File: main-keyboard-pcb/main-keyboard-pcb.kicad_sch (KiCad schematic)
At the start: 174 parts, among them IC1 LMR51420XDDCR, J1 Debug SWD Connector, J2 Hotplug, J3 USB_B_Micro, SW1 SW_Push, SW10 SW_Push, SW11 SW_Push, SW12 SW_Push, SW13 SW_Push, SW14 SW_Push, SW15 SW_Push, SW16 SW_Push, SW17 SW_Push, SW18 SW_Push, SW19 SW_Push, SW2 SW_Push, SW20 SW_Push, SW21 SW_Push, SW22 SW_Push, SW23 SW_Push, SW24 SW_Push, SW25 SW_Push, SW26 SW_Push, SW27 SW_Push, SW28 SW_Push, SW29 SW_Push, SW3 SW_Push, SW30 SW_Push, SW31 SW_Push, SW32 SW_Push, SW33 SW_Push, SW34 SW_Push, SW35 SW_Push, SW36 SW_Push, SW37 SW_Push, SW38 SW_Push, SW39 SW_Push, SW4 SW_Push, SW40 SW_Push, SW41 SW_Push, SW42 SW_Push, SW43 SW_Push, SW44 SW_Push, SW45 SW_Push, SW46 SW_Push, SW47 SW_Push, SW48 SW_Push, SW49 SW_Push, SW5 SW_Push, SW50 SW_Push, SW51 SW_Push, SW52 SW_Push, SW53 SW_Push, SW54 SW_Push, SW55 SW_Push, SW56 SW_Push, SW57 SW_Push, SW58 SW_Push, SW59 SW_Push, SW6 SW_Push, SW60 SW_Push, SW61 SW_Push, SW62 SW_Push, SW63 SW_Push, SW64 SW_Push, SW65 SW_Push, SW66 SW_Push, SW67 SW_Push, SW7 SW_Push, SW8 SW_Push, SW9 SW_Push, SW99 SW_SPDT, U1 USBLC6-4SC6, U2 STM32F407VGT6, Y1 16MHz

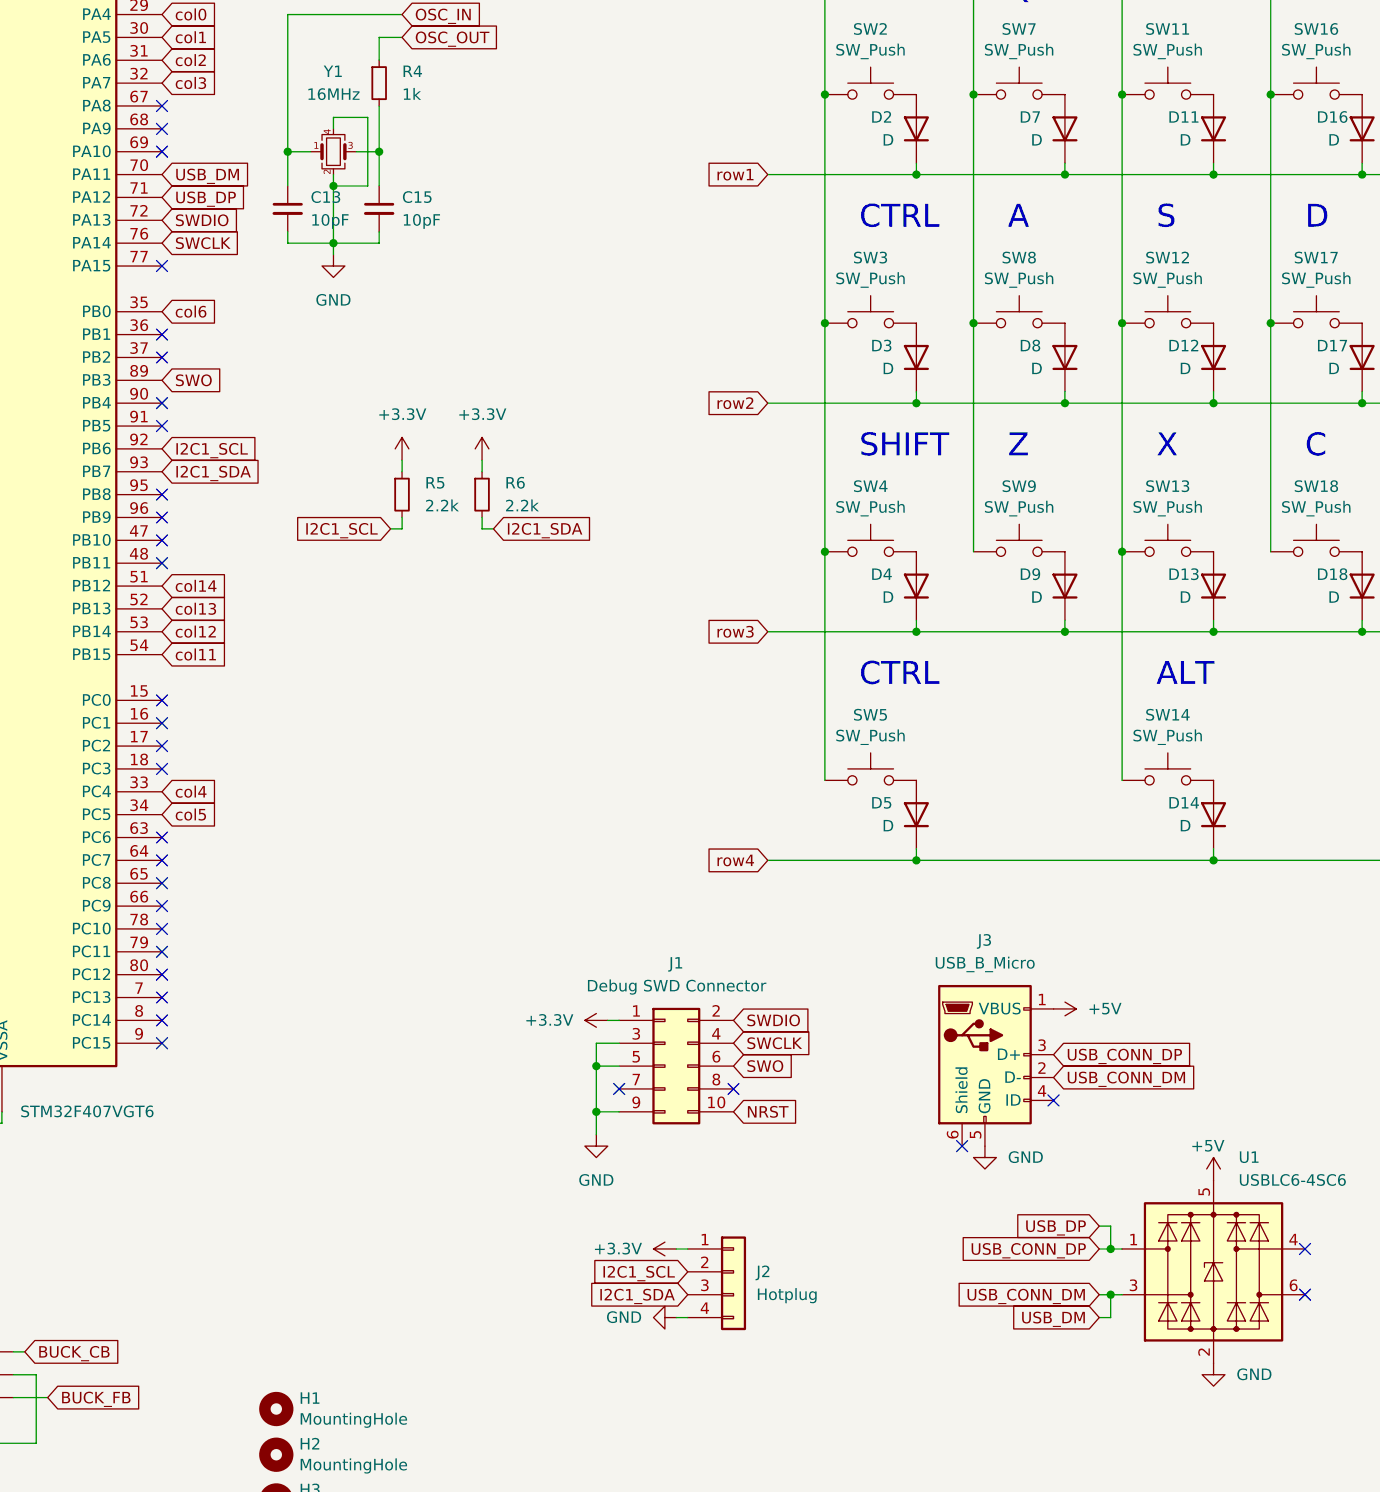
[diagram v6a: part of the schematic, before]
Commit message: Finished initial PCB design, spacing fixes needed
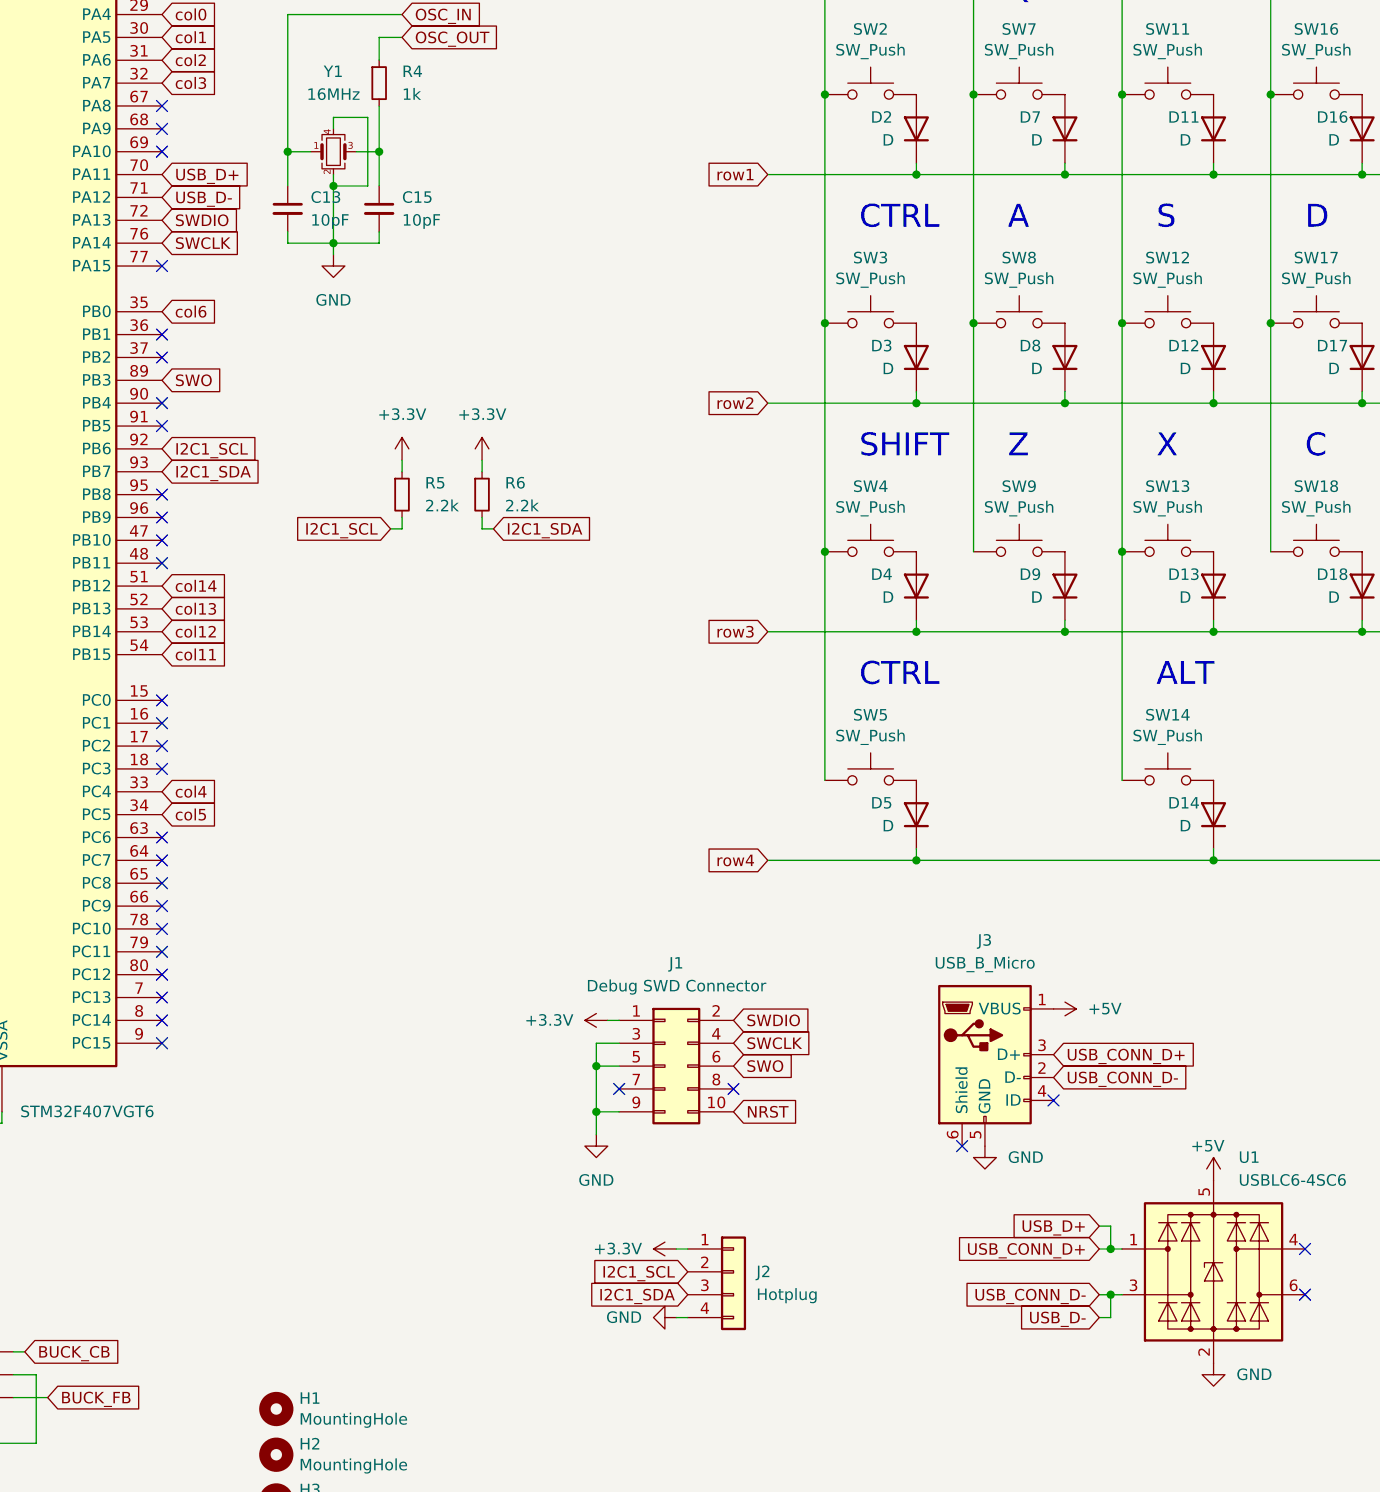
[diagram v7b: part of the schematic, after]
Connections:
- net USB_CONN_DM renamed USB_CONN_D-
- net USB_CONN_D-: now also U2.71 (PA12); no longer U2.70 (PA11)
- net USB_CONN_DP renamed USB_CONN_D+
- net USB_CONN_D+: now also U2.70 (PA11); no longer U2.71 (PA12)
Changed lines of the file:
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@@
     )
   )
-  (global_label "USB_CONN_DM" (shape input) (at 187.96 208.28 180) (fields_autoplaced)
-    (effects (font (size 1.27 1.27)) (justify right))
-    (property "Intersheet References" "${INTERSHEET_REFS}" (id 0) (at 171.8188 208.3594 0)
-      (effects (font (size 1.27 1.27)) (justify right) hide)
-    )
-  )
-  (global_label "USB_DP" (shape input) (at 187.96 200.66 180) (fields_autoplaced)
-    (effects (font (size 1.27 1.27)) (justify right))
-    (property "Intersheet References" "${INTERSHEET_REFS}" (id 0) (at 178.2293 200.7394 0)
-      (effects (font (size 1.27 1.27)) (justify right) hide)
-    )
-  )
-  (global_label "USB_CONN_DM" (shape input) (at 182.88 184.15 0) (fields_autoplaced)
-    (effects (font (size 1.27 1.27)) (justify left))
-    (property "Intersheet References" "${INTERSHEET_REFS}" (id 0) (at 199.0212 184.0706 0)
+  (global_label "USB_CONN_D-" (shape input) (at 187.96 208.28 180) (fields_autoplaced)
+    (effects (font (size 1.27 1.27)) (justify right))
+    (property "Intersheet References" "${INTERSHEET_REFS}" (id 0) (at 171.6979 208.2006 0)
+      (effects (font (size 1.27 1.27)) (justify right) hide)
+    )
+  )
+  (global_label "USB_D+" (shape input) (at 187.96 200.66 180) (fields_autoplaced)
+    (effects (font (size 1.27 1.27)) (justify right))
+    (property "Intersheet References" "${INTERSHEET_REFS}" (id 0) (at 177.9269 200.5806 0)
+      (effects (font (size 1.27 1.27)) (justify right) hide)
+    )
+  )
+  (global_label "USB_CONN_D-" (shape input) (at 182.88 184.15 0) (fields_autoplaced)
+    (effects (font (size 1.27 1.27)) (justify left))
+    (property "Intersheet References" "${INTERSHEET_REFS}" (id 0) (at 199.1421 184.0706 0)
       (effects (font (size 1.27 1.27)) (justify left) hide)
     )
@@
     )
   )
-  (global_label "USB_DM" (shape input) (at 187.96 210.82 180) (fields_autoplaced)
-    (effects (font (size 1.27 1.27)) (justify right))
-    (property "Intersheet References" "${INTERSHEET_REFS}" (id 0) (at 178.0479 210.8994 0)
+  (global_label "USB_D-" (shape input) (at 187.96 210.82 180) (fields_autoplaced)
+    (effects (font (size 1.27 1.27)) (justify right))
+    (property "Intersheet References" "${INTERSHEET_REFS}" (id 0) (at 177.9269 210.7406 0)
       (effects (font (size 1.27 1.27)) (justify right) hide)
     )
@@
     )
   )
-  (global_label "USB_CONN_DP" (shape input) (at 182.88 181.61 0) (fields_autoplaced)
-    (effects (font (size 1.27 1.27)) (justify left))
-    (property "Intersheet References" "${INTERSHEET_REFS}" (id 0) (at 198.8398 181.5306 0)
+  (global_label "USB_CONN_D+" (shape input) (at 182.88 181.61 0) (fields_autoplaced)
+    (effects (font (size 1.27 1.27)) (justify left))
+    (property "Intersheet References" "${INTERSHEET_REFS}" (id 0) (at 199.1421 181.5306 0)
       (effects (font (size 1.27 1.27)) (justify left) hide)
     )
@@
     )
   )
-  (global_label "USB_DM" (shape input) (at 83.82 83.82 0) (fields_autoplaced)
-    (effects (font (size 1.27 1.27)) (justify left))
-    (property "Intersheet References" "${INTERSHEET_REFS}" (id 0) (at 93.7321 83.7406 0)
+  (global_label "USB_D+" (shape input) (at 83.82 83.82 0) (fields_autoplaced)
+    (effects (font (size 1.27 1.27)) (justify left))
+    (property "Intersheet References" "${INTERSHEET_REFS}" (id 0) (at 93.8531 83.7406 0)
       (effects (font (size 1.27 1.27)) (justify left) hide)
     )
@@
     )
   )
-  (global_label "USB_CONN_DP" (shape input) (at 187.96 203.2 180) (fields_autoplaced)
-    (effects (font (size 1.27 1.27)) (justify right))
-    (property "Intersheet References" "${INTERSHEET_REFS}" (id 0) (at 172.0002 203.2794 0)
+  (global_label "USB_CONN_D+" (shape input) (at 187.96 203.2 180) (fields_autoplaced)
+    (effects (font (size 1.27 1.27)) (justify right))
+    (property "Intersheet References" "${INTERSHEET_REFS}" (id 0) (at 171.6979 203.1206 0)
       (effects (font (size 1.27 1.27)) (justify right) hide)
     )
@@
     )
   )
-  (global_label "USB_DP" (shape input) (at 83.82 86.36 0) (fields_autoplaced)
-    (effects (font (size 1.27 1.27)) (justify left))
-    (property "Intersheet References" "${INTERSHEET_REFS}" (id 0) (at 93.5507 86.2806 0)
-      (effects (font (size 1.27 1.27)) (justify left) hide)
-    )
+  (global_label "USB_D-" (shape input) (at 83.82 86.36 0) (fields_autoplaced)
+    (effects (font (size 1.27 1.27)) (justify left))
+    (property "Intersheet References" "${INTERSHEET_REFS}" (id 0) (at 93.8531 86.2806 0)
+      (effects (font (size 1.27 1.27)) (justify left) hide)
+    )

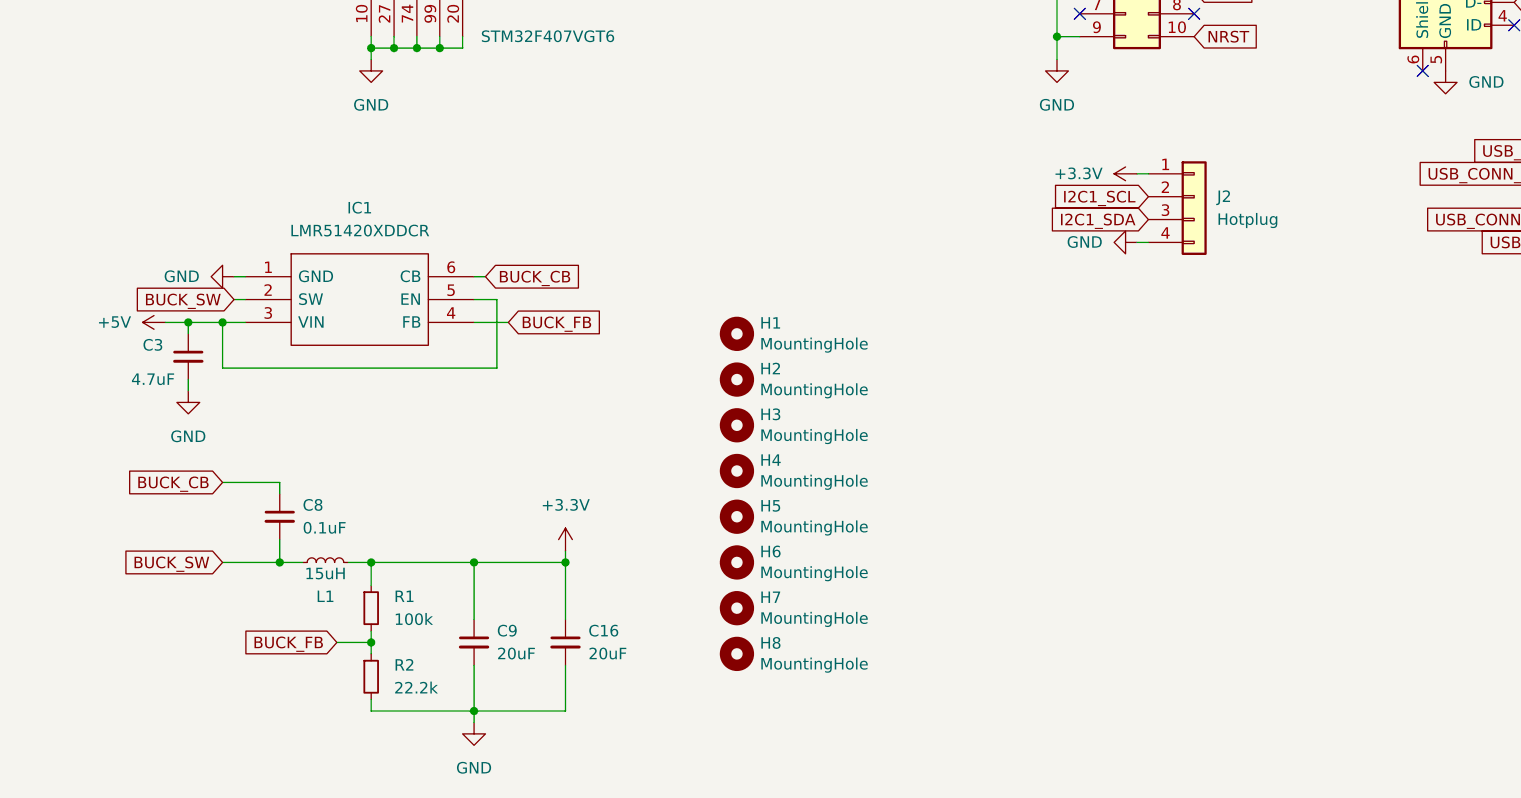
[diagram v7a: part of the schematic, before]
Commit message: Updated buck converter design to webench recommendation and updated caps to 0805
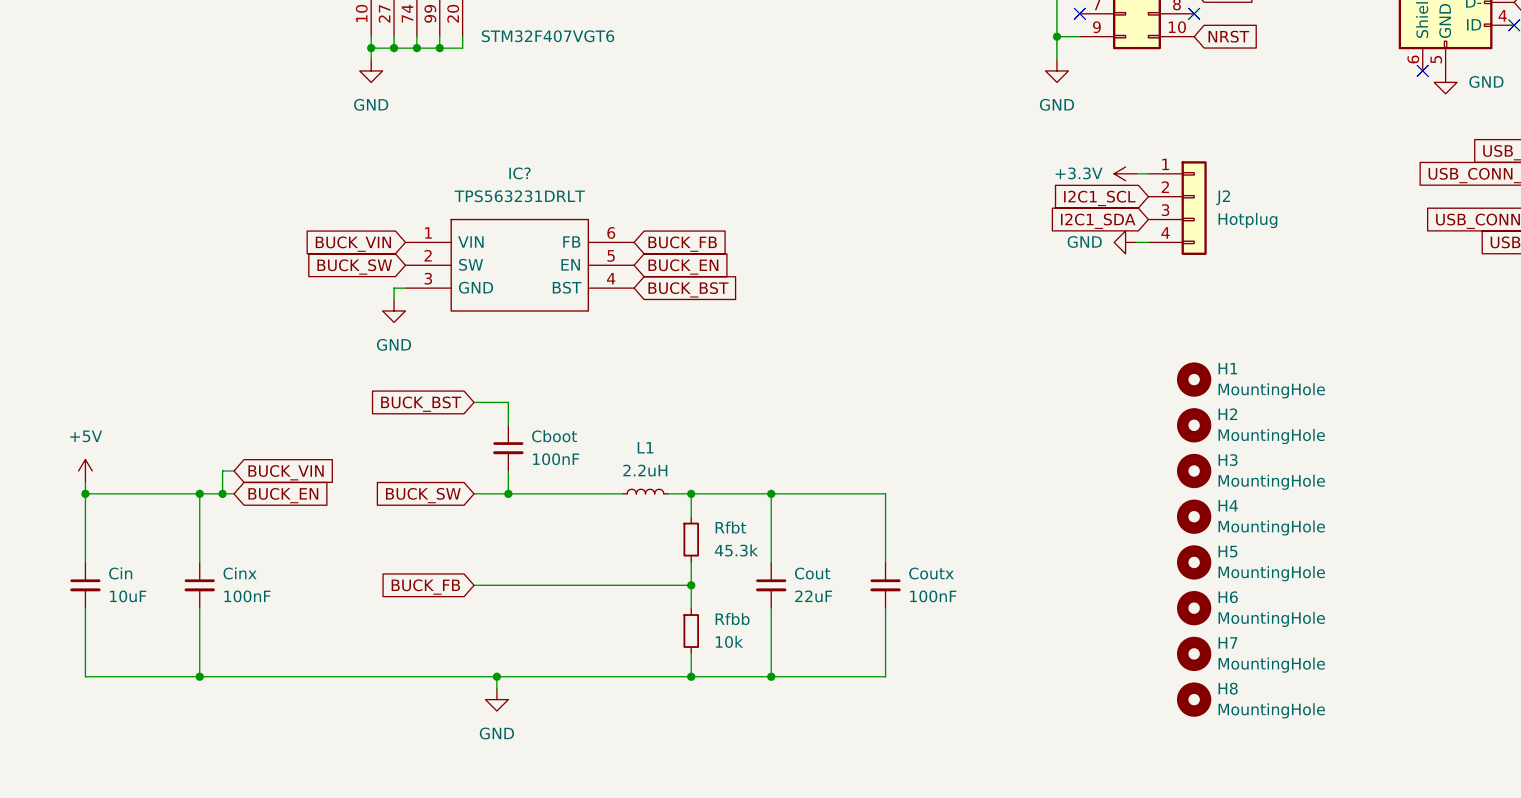
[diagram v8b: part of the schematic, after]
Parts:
- removed C16, C9: 20uF, buck-converter:GRMJN7R61C206ME05D, symbol Device:C_Small
- removed C3: 4.7uF, stm32f4_2:GRM188R61C475KAAJD, symbol Device:C_Small
- removed C8: 0.1uF, stm32f4_2:GRM022R61A104ME01L, symbol Device:C_Small
- removed IC1: LMR51420XDDCR, buck-converter:LMR51420XDDCR, symbol buck-converter:LMR51420XDDCR
- removed R1: 100k, buck-converter:CHV1206AJW-104ELF, symbol Device:R_Small
- removed R2: 22.2k, buck-converter:ERJP08F2212V, symbol Device:R_Small
- added Cboot, Cinx, Coutx: 100nF, symbol Device:C_Small
- added Cin: 10uF, symbol Device:C_Small
- added Cout: 22uF, symbol Device:C_Small
- added IC?: TPS563231DRLT, TPS563231DRLT, symbol buck-converter:TPS563231DRLT
- added Rfbb: 10k, symbol Device:R_Small
- added Rfbt: 45.3k, symbol Device:R_Small
- C1, C4: footprint stm32f4_2:GRM155R61E225KE11D -> stm32f4_2:08055C225KAT2A
- C10, C11, C12, C14, C17, C5, C6, C7: footprint stm32f4_2:GRM022R61A104ME01L -> stm32f4_2:C0805C104K5RAC7411
- C13, C15: footprint stm32f4_2:GRM0225C1C100FA03L -> stm32f4_2:C0805C100J2GACAUTO
- C2: footprint stm32f4_2:GRM188R61C475KAAJD -> stm32f4_2:C0805C475K3RACTU
- L1: value 15uH -> 2.2uH; footprint buck-converter:SRP1265WA150M -> (none)
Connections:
- net +3V3: no longer L1.2
- net +5V: now also Cin.1, Cinx.1, IC?.1 (VIN), IC?.5 (EN)
- net BUCK_FB: now also IC?.6 (FB), Rfbb.1, Rfbt.2
- net BUCK_SW: now also Cboot.2, IC?.2 (SW)
- net GND: now also Cin.2, Cinx.2, Cout.2, Coutx.2, IC?.3 (GND), Rfbb.2
- new net: Cout.1, Coutx.1, L1.2, Rfbt.1
- new net BUCK_BST: Cboot.1, IC?.4 (BST)
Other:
- moved on the sheet: H1, H2, H3, H4, H5, H6, H7, H8
